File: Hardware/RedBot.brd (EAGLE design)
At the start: 94 x 49.5 mm, 68 parts, among them U1 ATMEGA328P, U2 TB6612FNG, U3 MIC5219 5V, U4 MIC5219 3.3V, U5 FT232RLSSOP, U6 7408SE, Y1 16MHz

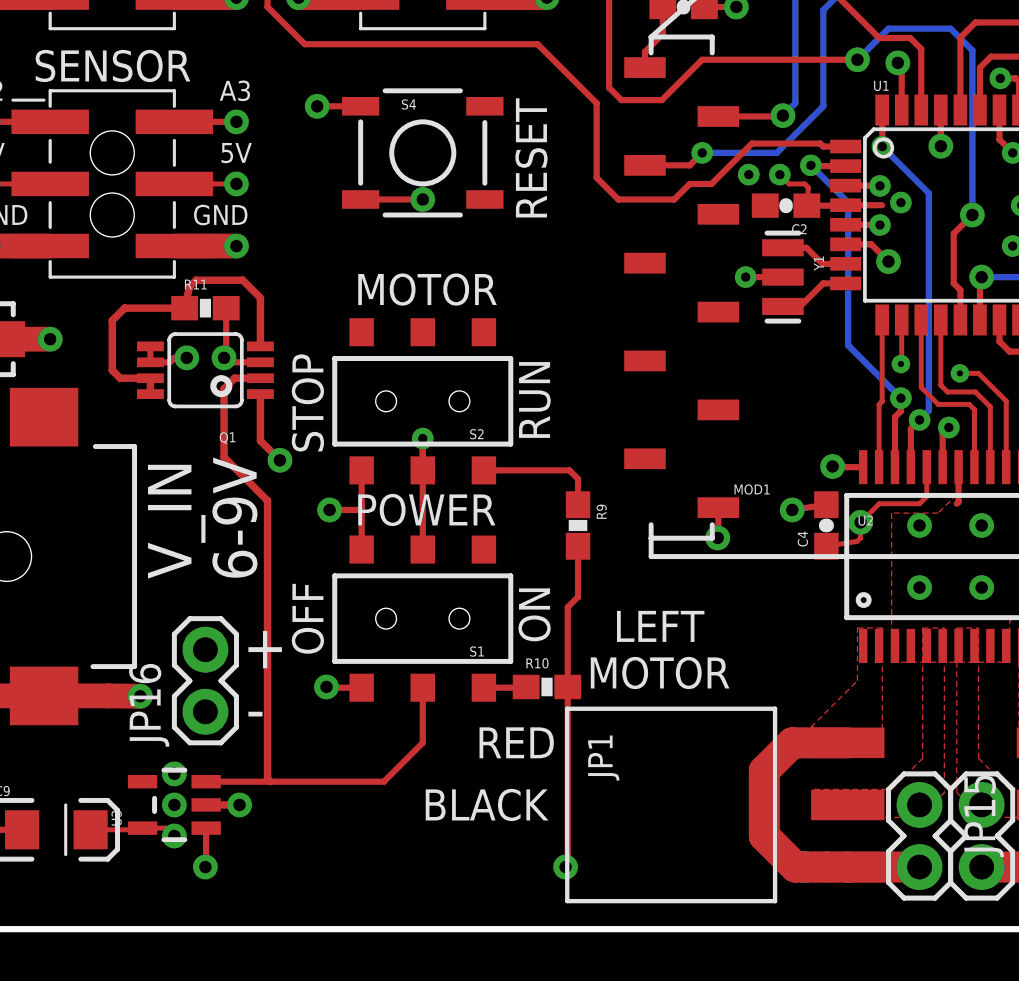
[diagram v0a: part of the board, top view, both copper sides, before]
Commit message: Added PTC to V_GATED
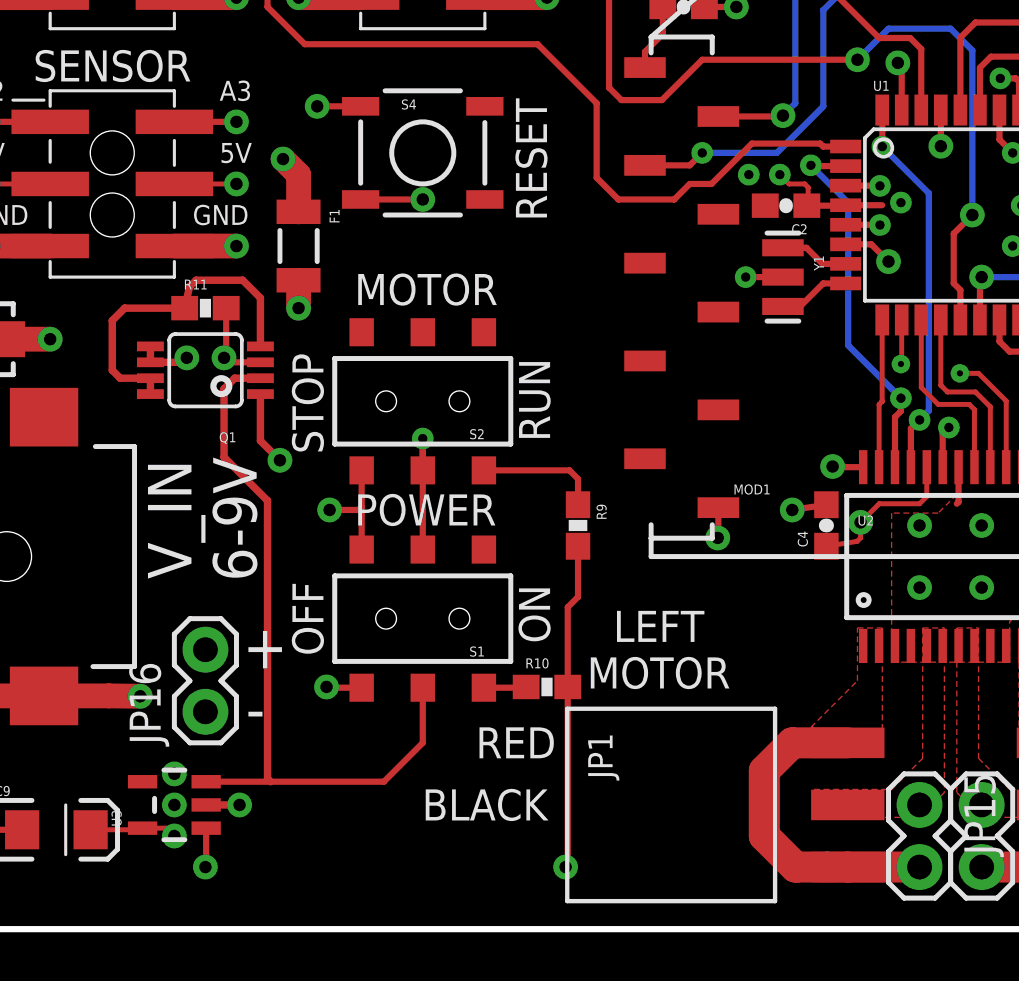
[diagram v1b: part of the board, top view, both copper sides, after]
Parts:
- added F1: PTCSMD, SparkFun-PowerIC:PTC-1206
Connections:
- new net N$9: F1.2, Q1.5, Q1.6
- net V_GATED: now also F1.1; no longer Q1.5, Q1.6
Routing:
- net V_GATED: track 117.2 -> 106.4 mm
- net N$9: track 0.00 -> 9.51 mm, vias 0 -> 2
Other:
- board text added: "v14"
- board text removed: "v13"
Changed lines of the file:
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@@
 <layers>
 <layer number="1" name="Top" color="4" fill="1" visible="yes" active="yes"/>
-<layer number="2" name="5V" color="1" fill="3" visible="no" active="yes"/>
-<layer number="15" name="Gnd" color="4" fill="6" visible="no" active="yes"/>
+<layer number="2" name="5V" color="1" fill="3" visible="yes" active="yes"/>
+<layer number="15" name="Gnd" color="4" fill="6" visible="yes" active="yes"/>
 <layer number="16" name="Bottom" color="1" fill="1" visible="yes" active="yes"/>
 <layer number="17" name="Pads" color="2" fill="1" visible="yes" active="yes"/>
@@
 <text x="294.64" y="37.973" size="1.27" layer="21" font="vector" ratio="15" align="center">POWER</text>
 <text x="302.387" y="18.034" size="0.8128" layer="21" font="vector" ratio="15" align="center">D13 LED</text>
-<text x="278.13" y="-3.81" size="1.27" layer="16" font="vector" ratio="15" rot="MR0" align="center">v13</text>
+<text x="278.13" y="-3.81" size="1.27" layer="16" font="vector" ratio="15" rot="MR0" align="center">v14</text>
 <text x="239.395" y="34.671" size="0.8128" layer="21" font="vector" ratio="15">5V</text>
 <text x="243.205" y="33.02" size="0.8128" layer="21" font="vector" ratio="15" align="center-left">GND</text>
@@
 </element>
 <element name="U$23" library="SparkFun-Aesthetics" package="REDBOT_LOGO" value="REDBOT_LOGO" x="302.006" y="5.08" rot="MR0"/>
+<element name="F1" library="SparkFun-PowerIC" package="PTC-1206" value="PTCSMD" x="256.54" y="21.59" rot="R270">
+<attribute name="PROD_ID" value="RES-11150" x="256.54" y="21.59" size="1.778" layer="27" font="vector" ratio="15" rot="R270" display="off"/>
+</element>
 </elements>
 <signals>
@@
 <contactref element="JP8" pad="4"/>
 <contactref element="JP9" pad="4"/>
-<via x="251.968" y="17.018" extent="1-16" drill="0.508"/>
-<wire x1="251.968" y1="17.018" x2="251.968" y2="18.288" width="1.016" layer="15"/>
-<wire x1="251.968" y1="18.288" x2="252.73" y2="19.05" width="1.016" layer="15"/>
-<wire x1="252.73" y1="19.05" x2="254.889" y2="19.05" width="1.016" layer="15"/>
-<wire x1="254.889" y1="19.05" x2="255.905" y2="20.066" width="1.016" layer="15"/>
-<wire x1="255.905" y1="20.066" x2="255.905" y2="29.718" width="1.016" layer="15"/>
+<wire x1="255.905" y1="25.146" x2="255.905" y2="29.718" width="1.016" layer="15"/>
 <wire x1="255.905" y1="29.718" x2="255.27" y2="30.353" width="1.016" layer="15"/>
 <wire x1="255.27" y1="30.353" x2="255.27" y2="33.02" width="1.016" layer="15"/>
@@
 <via x="266.7" y="34.29" extent="1-16" drill="0.508"/>
 <wire x1="266.7" y1="34.29" x2="266.7" y2="41.529" width="1.016" layer="2"/>
-<contactref element="Q1" pad="5"/>
-<contactref element="Q1" pad="6"/>
-<wire x1="251.968" y1="17.018" x2="251.46" y2="17.018" width="0.254" layer="1"/>
-<wire x1="251.46" y1="17.018" x2="251.277" y2="16.835" width="0.254" layer="1"/>
-<wire x1="250.48" y1="16.835" x2="251.277" y2="16.835" width="0.254" layer="1"/>
-<wire x1="250.48" y1="16.835" x2="250.48" y2="17.485" width="0.254" layer="1"/>
+<wire x1="256.54" y1="24.511" x2="255.905" y2="25.146" width="1.016" layer="1"/>
+<via x="255.905" y="25.146" extent="1-16" drill="0.508"/>
+<contactref element="F1" pad="1"/>
+<wire x1="256.54" y1="24.511" x2="256.54" y2="22.99" width="1.016" layer="1"/>
 </signal>
 <signal name="N$3">
@@
 <wire x1="310.73" y1="8.89" x2="312.051" y2="8.89" width="0.254" layer="1"/>
 </signal>
+<signal name="N$9">
+<contactref element="F1" pad="2"/>
+<contactref element="Q1" pad="6"/>
+<contactref element="Q1" pad="5"/>
+<wire x1="256.54" y1="20.19" x2="256.54" y2="19.05" width="1.016" layer="1"/>
+<via x="256.54" y="19.05" extent="1-16" drill="0.508"/>
+<wire x1="256.54" y1="19.05" x2="252.73" y2="19.05" width="1.016" layer="15"/>
+<wire x1="252.73" y1="19.05" x2="251.968" y2="18.288" width="1.016" layer="15"/>
+<wire x1="251.968" y1="18.288" x2="251.968" y2="17.018" width="1.016" layer="15"/>
+<via x="251.968" y="17.018" extent="1-16" drill="0.508"/>
+<wire x1="250.48" y1="17.485" x2="250.48" y2="16.835" width="0.3048" layer="1"/>
+<wire x1="250.48" y1="16.835" x2="251.785" y2="16.835" width="0.3048" layer="1"/>
+<wire x1="251.785" y1="16.835" x2="251.968" y2="17.018" width="0.3048" layer="1"/>
+</signal>
 </signals>
+<errors>
+</errors>
 </board>
 </drawing>
